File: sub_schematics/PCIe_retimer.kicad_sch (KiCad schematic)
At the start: 1 part, among them U1 DS160PT801ACBR

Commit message: buck converter
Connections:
- net PWR.1_8V: now reaches U1.AE12 (PWR_1)
- net PWR.1_8V: now also U1.AF11 (PWR_1), U1.AF13 (PWR_1), U1.AG10 (PWR_1), U1.AG14 (PWR_1), U1.AH11 (PWR_1), U1.AH13 (PWR_1), U1.AJ12 (PWR_1), U1.J12 (PWR_1), U1.K11 (PWR_1), U1.K13 (PWR_1), U1.L10 (PWR_1), U1.L14 (PWR_1), U1.M11 (PWR_1), U1.M13 (PWR_1), U1.N12 (PWR_1)
- net PWR.1_17V: now reaches U1.AA12 (PWR2_HS_D)
- net PWR.1_17V: now also U1.AB15 (PWR_2_A), U1.AB17 (PWR_2_A), U1.AB7 (PWR2_HS_A), U1.AB9 (PWR2_HS_A), U1.AC10 (PWR2_HS_D), U1.AC14 (PWR_2_A), U1.AD15 (PWR_2_A), U1.AD17 (PWR_2_A), U1.AD7 (PWR2_HS_A), U1.AD9 (PWR2_HS_A), U1.AK15 (PWR2_HS_D), U1.AK17 (PWR2_HS_A), U1.AK7 (PWR2_HS_A), U1.AK9 (PWR2_HS_D), U1.AL10 (PWR2_HS_D), U1.AL14 (PWR2_HS_D), U1.AM15 (PWR2_HS_D), U1.AM17 (PWR2_HS_A), U1.AM7 (PWR2_HS_A), U1.AM9 (PWR2_HS_D), U1.F15 (PWR2_HS_D), U1.F17 (PWR2_HS_A), U1.F7 (PWR2_HS_A), U1.F9 (PWR2_HS_D), U1.G10 (PWR2_HS_D), U1.G14 (PWR2_HS_D), U1.H15 (PWR2_HS_D), U1.H17 (PWR2_HS_A), U1.H7 (PWR2_HS_A), U1.H9 (PWR2_HS_D), U1.P15 (PWR2_HS_A), U1.P17 (PWR2_HS_A), U1.P7 (PWR_2_A), U1.P9 (PWR_2_A), U1.R10 (PWR_2_A), U1.R14 (PWR2_HS_D), U1.T15 (PWR2_HS_A), U1.T17 (PWR2_HS_A), U1.T7 (PWR_2_A), U1.T9 (PWR_2_A), U1.U12 (PWR2_HS_D), U1.V11 (PWR2_HS_D), U1.V13 (PWR2_HS_A), U1.W10 (PWR2_HS_A), U1.W14 (PWR2_HS_A), U1.Y11 (PWR2_HS_A), U1.Y13 (PWR2_HS_D)
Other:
- sheet PCIe_retimer_power ports: added PWR{1_8V 1_17V}, PWR{3V3 5V}; removed none
- moved on the sheet: U1C, U1F

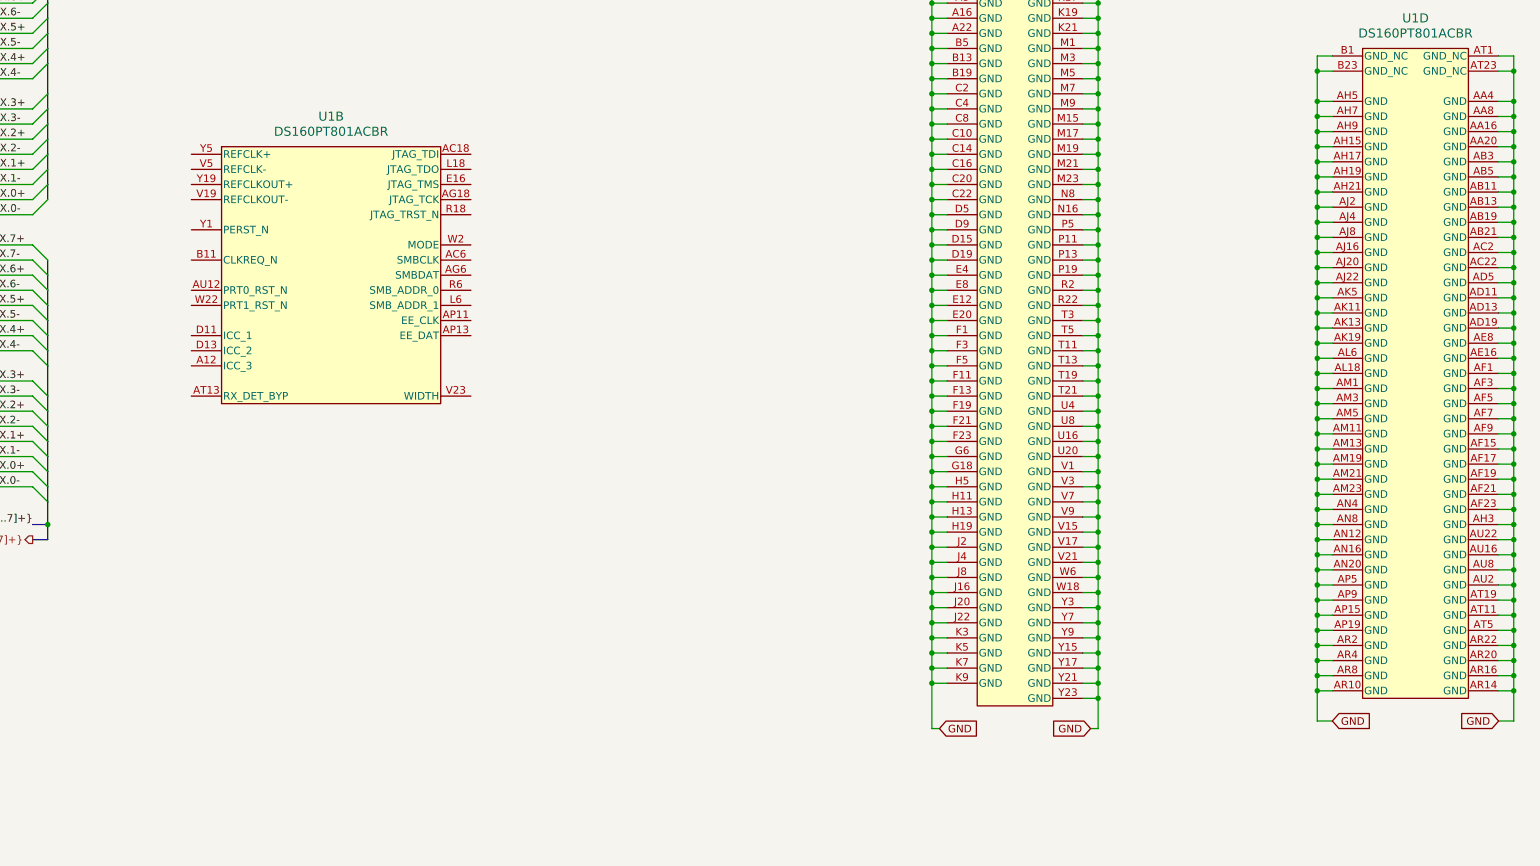
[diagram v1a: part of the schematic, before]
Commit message: Schematics revamped
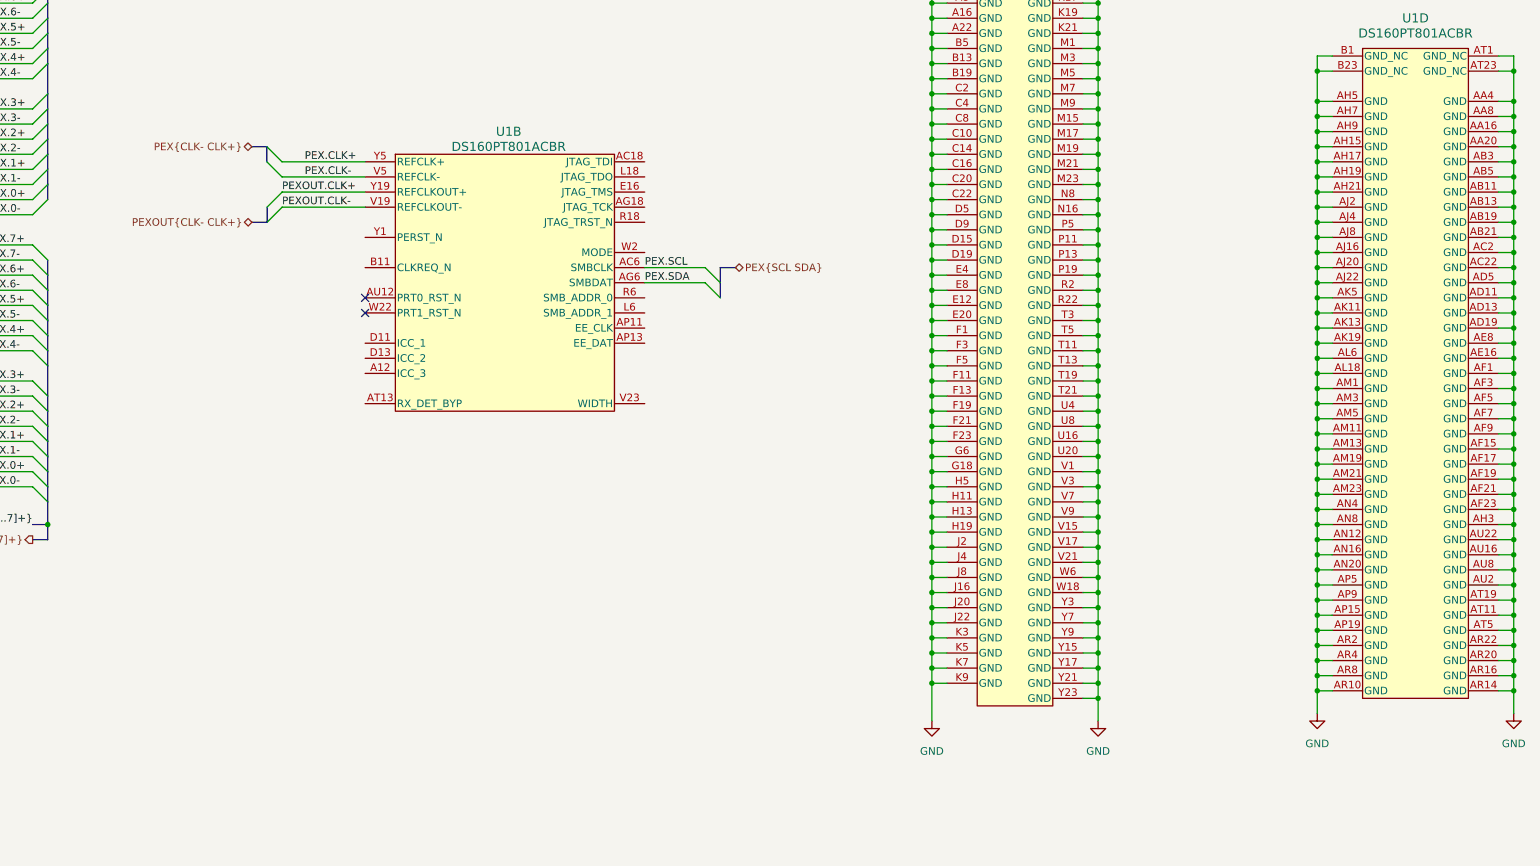
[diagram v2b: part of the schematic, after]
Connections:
- net PEX.SCL: now reaches U1.AC6 (SMBCLK)
- net PEX.SDA: now reaches U1.AG6 (SMBDAT)
- net PEXOUT.CLK-: now reaches U1.V19 (REFCLKOUT-)
- net PEX.CLK-: now reaches U1.V5 (REFCLK-)
- net PEXOUT.CLK+: now reaches U1.Y19 (REFCLKOUT+)
- net PEX.CLK+: now reaches U1.Y5 (REFCLK+)
- no-connect marks 0 -> 2
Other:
- moved on the sheet: U1B

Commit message: PCIe shematic fix
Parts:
- added C1, C10, C11, C12, C13, C14, C15, C16, C17, C18, C19, C2, C20, C21, C22, C23, C24, C25, C26, C27, C28, C29, C3, C30, C31, C32, C33, C34, C35, C36, C37, C38, C39, C4, C40, C41, C42, C43, C44, C45, C46, C47, C48, C49, C5, C50, C51, C52, C53, C54, C55, C56, C57, C58, C59, C6, C60, C61, C62, C63, C64, C7, C8, C9: 0201_885012104006, WE_WCAP-CSGP:C_Wurth_WCAP-CSGP-0201, symbol WE_WCAP-CSGP:0201_885012104006
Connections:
- net A_RX.0+: now also U1.AK21 (A_PEX_RX7N), C47.1; no longer U1.B15 (A_PEX_RX0P)
- net A_RX.0-: now also U1.AL20 (A_PEX_RX7P), C48.1; no longer U1.A14 (A_PEX_RX0N)
- net A_RX.1+: now also U1.AG22 (A_PEX_RX6N), C45.1; no longer U1.C18 (A_PEX_RX1P)
- net A_RX.1-: now also U1.AH23 (A_PEX_RX6P), C46.1; no longer U1.D17 (A_PEX_RX1N)
- net A_RX.2+: now also U1.AD21 (A_PEX_RX5N), C43.1; no longer U1.B21 (A_PEX_RX2P)
- net A_RX.2-: now also U1.AE20 (A_PEX_RX5P), C44.1; no longer U1.A20 (A_PEX_RX2N)
- net A_RX.3+: now also U1.AA22 (A_PEX_RX4N), C41.1; no longer U1.E22 (A_PEX_RX3P)
- net A_RX.3-: now also U1.AB23 (A_PEX_RX4P), C42.1; no longer U1.D23 (A_PEX_RX3N)
- net A_RX.4+: now also U1.D23 (A_PEX_RX3N), C39.1; no longer U1.AB23 (A_PEX_RX4P)
- net A_RX.4-: now also U1.E22 (A_PEX_RX3P), C40.1; no longer U1.AA22 (A_PEX_RX4N)
- net A_RX.5+: now also U1.A20 (A_PEX_RX2N), C37.1; no longer U1.AE20 (A_PEX_RX5P)
- net A_RX.5-: now also U1.B21 (A_PEX_RX2P), C38.1; no longer U1.AD21 (A_PEX_RX5N)
- net A_RX.6+: now also U1.D17 (A_PEX_RX1N), C35.1; no longer U1.AH23 (A_PEX_RX6P)
- net A_RX.6-: now also U1.C18 (A_PEX_RX1P), C36.1; no longer U1.AG22 (A_PEX_RX6N)
- net A_RX.7+: now also U1.A14 (A_PEX_RX0N), C33.1; no longer U1.AL20 (A_PEX_RX7P)
- net A_RX.7-: now also U1.B15 (A_PEX_RX0P), C34.1; no longer U1.AK21 (A_PEX_RX7N)
- net A_TX.0+: now also C2.1
- net A_TX.0-: now also C1.1
- net A_TX.1+: now also C4.1
- net A_TX.1-: now also C3.1
- net A_TX.2+: now also C6.1
- net A_TX.2-: now also C5.1
- net A_TX.3+: now also C8.1
- net A_TX.3-: now also C7.1
- net A_TX.4+: now also C10.1
- net A_TX.4-: now also C9.1
- net A_TX.5+: now also C12.1
- net A_TX.5-: now also C11.1
- net A_TX.6+: now also C14.1
- net A_TX.6-: now also C13.1
- net A_TX.7+: now also C16.1
- net A_TX.7-: now also C15.1
- net B_RX.0+: now also U1.H3 (B_PEX_RX0P), C50.1; no longer U1.H21 (B_PEX_TX0P)
- net B_RX.0-: now also U1.G4 (B_PEX_RX0N), C49.1; no longer U1.G20 (B_PEX_TX0N)
- net B_RX.1+: now also U1.L2 (B_PEX_RX1P), C52.1; no longer U1.L22 (B_PEX_TX1P)
- net B_RX.1-: now also U1.K1 (B_PEX_RX1N), C51.1; no longer U1.K23 (B_PEX_TX1N)
- net B_RX.2+: now also U1.P3 (B_PEX_RX2P), C54.1; no longer U1.P21 (B_PEX_TX2P)
- net B_RX.2-: now also U1.N4 (B_PEX_RX2N), C53.1; no longer U1.N20 (B_PEX_TX2N)
- net B_RX.3+: now also U1.U2 (B_PEX_RX3P), C56.1; no longer U1.U22 (B_PEX_TX3P)
- net B_RX.3-: now also U1.T1 (B_PEX_RX3N), C55.1; no longer U1.T23 (B_PEX_TX3N)
- net B_RX.4+: now also U1.AP1 (B_PEX_RX4P), C58.1; no longer U1.AP23 (B_PEX_TX4P)
- net B_RX.4-: now also U1.AN2 (B_PEX_RX4N), C57.1; no longer U1.AN22 (B_PEX_TX4N)
- net B_RX.5+: now also U1.AU4 (B_PEX_RX5P), C60.1; no longer U1.AU20 (B_PEX_TX4P)
- net B_RX.5-: now also U1.AT3 (B_PEX_RX5N), C59.1; no longer U1.AT21 (B_PEX_TX5N)
- net B_RX.6+: now also U1.AP7 (B_PEX_RX6P), C62.1; no longer U1.AP17 (B_PEX_TX6P)
- net B_RX.6-: now also U1.AR6 (B_PEX_RX6N), C61.1; no longer U1.AR18 (B_PEX_TX6N)
- net B_RX.7+: now also U1.AU10 (B_PEX_RX7P), C64.1; no longer U1.AU14 (B_PEX_TX7P)
- net B_RX.7-: now also U1.AT9 (B_PEX_RX7N), C63.1; no longer U1.AT15 (B_PEX_TX7N)
- net B_TX.0+: now also U1.H21 (B_PEX_TX0P), C18.1; no longer U1.H3 (B_PEX_RX0P)
- net B_TX.0-: now also U1.G20 (B_PEX_TX0N), C17.1; no longer U1.G4 (B_PEX_RX0N)
- net B_TX.1+: now also U1.L22 (B_PEX_TX1P), C20.1; no longer U1.L2 (B_PEX_RX1P)
- net B_TX.1-: now also U1.K23 (B_PEX_TX1N), C19.1; no longer U1.K1 (B_PEX_RX1N)
- net B_TX.2+: now also U1.P21 (B_PEX_TX2P), C22.1; no longer U1.P3 (B_PEX_RX2P)
- net B_TX.2-: now also U1.N20 (B_PEX_TX2N), C21.1; no longer U1.N4 (B_PEX_RX2N)
- net B_TX.3+: now also U1.U22 (B_PEX_TX3P), C24.1; no longer U1.U2 (B_PEX_RX3P)
- net B_TX.3-: now also U1.T23 (B_PEX_TX3N), C23.1; no longer U1.T1 (B_PEX_RX3N)
- net B_TX.4+: now also U1.AP23 (B_PEX_TX4P), C26.1; no longer U1.AP1 (B_PEX_RX4P)
- net B_TX.4-: now also U1.AN22 (B_PEX_TX4N), C25.1; no longer U1.AN2 (B_PEX_RX4N)
- net B_TX.5+: now also U1.AU20 (B_PEX_TX4P), C28.1; no longer U1.AU4 (B_PEX_RX5P)
- net B_TX.5-: now also U1.AT21 (B_PEX_TX5N), C27.1; no longer U1.AT3 (B_PEX_RX5N)
- net B_TX.6+: now also U1.AP17 (B_PEX_TX6P), C30.1; no longer U1.AP7 (B_PEX_RX6P)
- net B_TX.6-: now also U1.AR18 (B_PEX_TX6N), C29.1; no longer U1.AR6 (B_PEX_RX6N)
- net B_TX.7+: now also U1.AU14 (B_PEX_TX7P), C32.1; no longer U1.AU10 (B_PEX_RX7P)
- net B_TX.7-: now also U1.AT15 (B_PEX_TX7N), C31.1; no longer U1.AT9 (B_PEX_RX7N)

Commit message: Switch to retimer for only clock
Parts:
- removed C1, C10, C11, C12, C13, C14, C15, C16, C17, C18, C19, C2, C20, C21, C22, C23, C24, C25, C26, C27, C28, C29, C3, C30, C31, C32, C33, C34, C35, C36, C37, C38, C39, C4, C40, C41, C42, C43, C44, C45, C46, C47, C48, C49, C5, C50, C51, C52, C53, C54, C55, C56, C57, C58, C59, C6, C60, C61, C62, C63, C64, C7, C8, C9: 0201_885012104006, WE_WCAP-CSGP:C_Wurth_WCAP-CSGP-0201, symbol WE_WCAP-CSGP:0201_885012104006
- removed U1: DS160PT801ACBR, pcie-redriver:ACB0332A-MFG, symbol pcie-redriver:DS160PT801ACBR
- added C1, C2, C4, C5: 0201_885012004001, WE_WCAP-CSGP:C_Wurth_WCAP-CSGP-0201, symbol WE_WCAP-CSGP:0201_885012004001
- added C3: 0402_885012105020, Capacitor_SMD_Wurth:C_Wurth_WCAP-CSGP-0402, symbol WE_WCAP-CSGP:0402_885012105020
- added U1: SY75602ATWL-TR, pcie-clk-mux:VDFN8_NNC_MCH, symbol pcie-clk-mux:SY75602ATWL-TR
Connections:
- net GND: now also U1.5 (GND)
- net PEX.CLK+: now also C1.2
- net PEX.CLK-: now also C2.2
- new net: C5.2, U1.7 (OUT1_N)
- new net: C4.1, U1.6 (OUT1_P)
- new net: C1.1, U1.1 (IN_P)
- new net: C3.2, U1.8 (VDD)
- new net: C2.1, U1.2 (IN_N)
- new net PEX_RETIME.CLK+: C4.2
- new net PEX_RETIME.CLK-: C5.1
- new net PWR.3V3: C3.1
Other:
- removed sheet PCIe_retimer_power

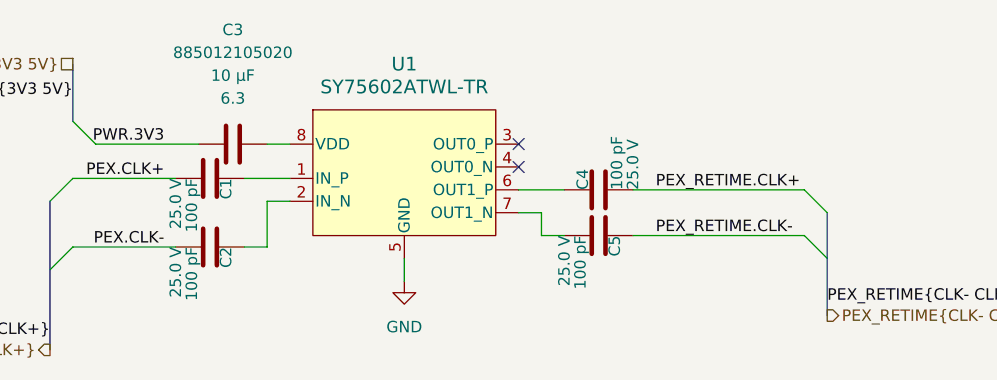
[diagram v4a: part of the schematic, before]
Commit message: Fixed board dimensions
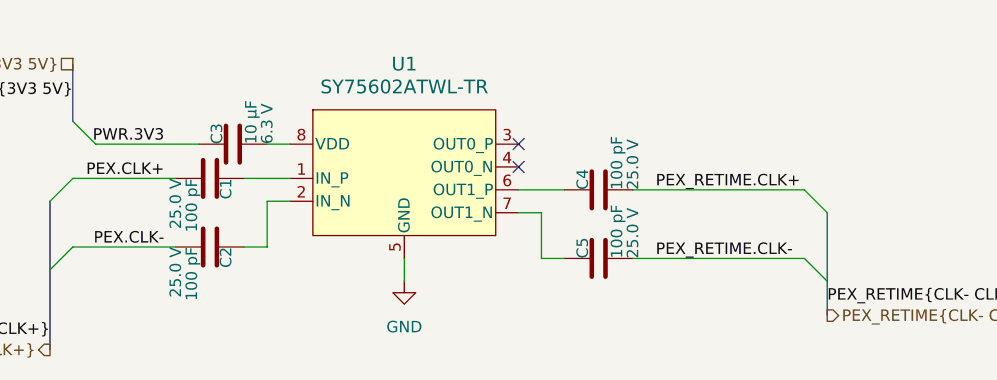
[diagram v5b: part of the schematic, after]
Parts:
- C3: footprint Capacitor_SMD_Wurth:C_Wurth_WCAP-CSGP-0402 -> WE_WCAP-CSGP:C_Wurth_WCAP-CSGP-0402; Voltage 6.3 -> 6.3 V
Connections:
- net PEX_RETIME.CLK-: now also C5.2; no longer C5.1
- net at U1.7 (OUT1_N): now also C5.1; no longer C5.2
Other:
- moved on the sheet: C5
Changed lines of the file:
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@@
 	)
 	(bus_entry
-		(at 228.6 177.8)
+		(at 228.6 180.34)
 		(size 2.54 2.54)
 		(stroke
@@
 	(wire
 		(pts
-			(xy 209.55 177.8) (xy 228.6 177.8)
+			(xy 209.55 180.34) (xy 228.6 180.34)
 		)
 		(stroke
@@
 	(wire
 		(pts
+			(xy 201.93 180.34) (xy 199.39 180.34)
+		)
+		(stroke
+			(width 0)
+			(type default)
+		)
+	)
+	(wire
+		(pts
 			(xy 168.91 173.99) (xy 171.45 173.99)
 		)
@@
 		)
 	)
+	(wire
+		(pts
+			(xy 199.39 175.26) (xy 196.85 175.26)
+		)
+		(stroke
+			(width 0)
+			(type default)
+		)
+	)
 	(bus
 		(pts
@@
 	(wire
 		(pts
-			(xy 199.39 177.8) (xy 199.39 175.26)
+			(xy 147.32 171.45) (xy 158.75 171.45)
 		)
 		(stroke
@@
 	(wire
 		(pts
-			(xy 201.93 177.8) (xy 199.39 177.8)
+			(xy 147.32 179.07) (xy 158.75 179.07)
+		)
+		(stroke
+			(width 0)
+			(type default)
+		)
+	)
+	(bus
+		(pts
+			(xy 147.32 165.1) (xy 147.32 158.75)
 		)
 		(stroke
@@
 	(wire
 		(pts
-			(xy 147.32 171.45) (xy 158.75 171.45)
+			(xy 209.55 172.72) (xy 228.6 172.72)
+		)
+		(stroke
+			(width 0)
+			(type default)
+		)
+	)
+	(wire
+		(pts
+			(xy 199.39 180.34) (xy 199.39 175.26)
+		)
+		(stroke
+			(width 0)
+			(type default)
+		)
+	)
+	(wire
+		(pts
+			(xy 166.37 179.07) (xy 168.91 179.07)
+		)
+		(stroke
+			(width 0)
+			(type default)
+		)
+	)
+	(wire
+		(pts
+			(xy 149.86 167.64) (xy 161.29 167.64)
+		)
+		(stroke
+			(width 0)
+			(type default)
+		)
+	)
+	(wire
+		(pts
+			(xy 168.91 179.07) (xy 168.91 173.99)
 		)
 		(stroke
@@
 		(pts
 			(xy 231.14 175.26) (xy 231.14 186.69)
-		)
-		(stroke
-			(width 0)
-			(type default)
-		)
-	)
-	(wire
-		(pts
-			(xy 147.32 179.07) (xy 158.75 179.07)
-		)
-		(stroke
-			(width 0)
-			(type default)
-		)
-	)
-	(bus
-		(pts
-			(xy 147.32 165.1) (xy 147.32 158.75)
-		)
-		(stroke
-			(width 0)
-			(type default)
-		)
-	)
-	(wire
-		(pts
-			(xy 209.55 172.72) (xy 228.6 172.72)
-		)
-		(stroke
-			(width 0)
-			(type default)
-		)
-	)
-	(wire
-		(pts
-			(xy 196.85 175.26) (xy 199.39 175.26)
-		)
-		(stroke
-			(width 0)
-			(type default)
-		)
-	)
-	(wire
-		(pts
-			(xy 166.37 179.07) (xy 168.91 179.07)
-		)
-		(stroke
-			(width 0)
-			(type default)
-		)
-	)
-	(wire
-		(pts
-			(xy 149.86 167.64) (xy 161.29 167.64)
-		)
-		(stroke
-			(width 0)
-			(type default)
-		)
-	)
-	(wire
-		(pts
-			(xy 168.91 179.07) (xy 168.91 173.99)
 		)
 		(stroke
@@
 	)
 	(label "PEX_RETIME.CLK-"
-		(at 212.09 177.8 0)
+		(at 212.09 180.34 0)
 		(effects
 			(font
@@
 	(symbol
 		(lib_id "WE_WCAP-CSGP:0201_885012004001")
-		(at 205.74 177.8 270)
+		(at 205.74 180.34 90)
 		(unit 1)
 		(body_style 1)
@@
 		(fields_autoplaced yes)
 		(property "Reference" "C5"
-			(at 207.518 177.8 0)
+			(at 203.962 180.34 0)
 			(show_name no)
 			(do_not_autoplace yes)
@@
 		)
 		(property "Value" "0201_885012004001"
-			(at 228.6 182.88 0)
+			(at 182.88 175.26 0)
 			(hide yes)
 			(show_name no)
@@
 		)
 		(property "Footprint" "WE_WCAP-CSGP:C_Wurth_WCAP-CSGP-0201"
-			(at 226.06 182.88 0)
+			(at 185.42 175.26 0)
 			(hide yes)
 			(show_name no)
@@
 		)
 		(property "Datasheet" "https://www.we-online.com/catalog/datasheet/885012004001.pdf?ki"
-			(at 223.52 182.88 0)
+			(at 187.96 175.26 0)
 			(hide yes)
 			(show_name no)
@@
 		)
 		(property "Description" "MLCCs 25 V(DC)"
-			(at 205.74 177.8 0)
+			(at 205.74 180.34 0)
 			(hide yes)
 			(show_name no)
@@
 		)
 		(property "Manufacturer" "Wurth Elektronik"
-			(at 220.98 182.88 0)
+			(at 190.5 175.26 0)
 			(hide yes)
 			(show_name no)
@@
 		)
 		(property "Manufacturer URL" "https://www.we-online.com"
-			(at 218.44 182.88 0)
+			(at 193.04 175.26 0)
 			(hide yes)
 			(show_name no)
@@
 		)
 		(property "Published Date" "20251008"
-			(at 215.9 182.88 0)
+			(at 195.58 175.26 0)
 			(hide yes)
 			(show_name no)
@@
 		)
 		(property "Match Code" "WCAP-CSGP"
-			(at 213.36 182.88 0)
+			(at 198.12 175.26 0)
 			(hide yes)
 			(show_name no)
@@
 		)
 		(property "Size" "0201"
-			(at 210.82 182.88 0)
+			(at 200.66 175.26 0)
 			(hide yes)
 			(show_name no)
@@
 		)
 		(property "Mounting Technology" "SMT"
-			(at 208.28 182.88 0)
+			(at 203.2 175.26 0)
 			(hide yes)
 			(show_name no)
@@
 		)
 		(property "Part Number" "885012004001"
-			(at 208.28 182.88 0)
+			(at 203.2 175.26 0)
 			(hide yes)
 			(show_name no)
@@
 		)
 		(property "Capacitance" "100 pF"
-			(at 203.708 177.8 0)
+			(at 207.772 180.34 0)
 			(show_name no)
 			(do_not_autoplace yes)
@@
 		)
 		(property "Voltage" "25.0 V"
-			(at 201.93 177.8 0)
+			(at 209.55 180.34 0)
 			(show_name no)
 			(do_not_autoplace yes)
@@
 		)
 		(property "C" "100 pF"
-			(at 203.2 190.5 0)
+			(at 208.28 167.64 0)
 			(hide yes)
 			(show_name no)
@@
 		)
 		(property "Tol. C" "±5%"
-			(at 200.66 190.5 0)
+			(at 210.82 167.64 0)
 			(hide yes)
 			(show_name no)
@@
 		)
 		(property "VR (V (DC))" "25.0"
-			(at 198.12 190.5 0)
+			(at 213.36 167.64 0)
 			(hide yes)
 			(show_name no)
@@
 		)
 		(property "Operating Temperature" "-55 °C up to +125 °C"
-			(at 195.58 190.5 0)
+			(at 215.9 167.64 0)
 			(hide yes)
 			(show_name no)
@@
 		)
 		(property "DF (%)" "–"
-			(at 193.04 190.5 0)
+			(at 218.44 167.64 0)
 			(hide yes)
 			(show_name no)
@@
 		)
 		(property "RISO" "10 GΩ"
-			(at 190.5 190.5 0)
+			(at 220.98 167.64 0)
 			(hide yes)
 			(show_name no)
@@
 		)
 		(property "Ceramic Type" "NP0 Class I"
-			(at 187.96 190.5 0)
+			(at 223.52 167.64 0)
 			(hide yes)
 			(show_name no)
@@
 		)
 		(property "L (mm)" "0.6"
-			(at 185.42 190.5 0)
+			(at 226.06 167.64 0)
 			(hide yes)
 			(show_name no)
@@
 		)
 		(property "W (mm)" "0.3"
-			(at 182.88 190.5 0)
+			(at 228.6 167.64 0)
 			(hide yes)
 			(show_name no)
@@
 		)
 		(property "H (mm)" "0.3"
-			(at 180.34 190.5 0)
+			(at 231.14 167.64 0)
 			(hide yes)
 			(show_name no)
@@
 		)
 		(property "Fl (mm)" "0.15"
-			(at 177.8 190.5 0)
+			(at 233.68 167.64 0)
 			(hide yes)
 			(show_name no)
@@
 		)
 		(property "Q (%)" "1000"
-			(at 175.26 190.5 0)
+			(at 236.22 167.64 0)
 			(hide yes)
 			(show_name no)
@@
 		)
 		(property "Demoboard" "nan"
-			(at 172.72 190.5 0)
+			(at 238.76 167.64 0)
 			(hide yes)
 			(show_name no)
@@
 		)
 		(property "Critical Parameter" ""
-			(at 198.12 177.8 0)
+			(at 213.36 180.34 0)
 			(show_name no)
 			(do_not_autoplace no)
@@
 		(fields_autoplaced yes)
 		(property "Reference" "C3"
-			(at 165.1 154.94 90)
-			(show_name no)
-			(do_not_autoplace no)
-			(effects
-				(font
-					(size 1.27 1.27)
-				)
+			(at 163.322 167.64 0)
+			(show_name no)
+			(do_not_autoplace yes)
+			(effects
+				(font
+					(size 1.27 1.27)
+				)
+				(justify left)
 			)
 		)
@@
 			)
 		)
-		(property "Footprint" "Capacitor_SMD_Wurth:C_Wurth_WCAP-CSGP-0402"
+		(property "Footprint" "WE_WCAP-CSGP:C_Wurth_WCAP-CSGP-0402"
 			(at 144.78 162.56 0)
 			(hide yes)
@@
 		)
 		(property "Part Number" "885012105020"
-			(at 165.1 157.48 90)
-			(show_name no)
-			(do_not_autoplace no)
-			(effects
-				(font
-					(size 1.27 1.27)
-				)
+			(at 162.56 162.56 0)
+			(hide yes)
+			(show_name no)
+			(do_not_autoplace no)
+			(effects
+				(font
+					(size 1.27 1.27)
+				)
+				(justify left)
 			)
 		)
 		(property "Capacitance" "10 µF"
-			(at 165.1 160.02 90)
-			(show_name no)
-			(do_not_autoplace no)
-			(effects
-				(font
-					(size 1.27 1.27)
-				)
-			)
-		)
-		(property "Voltage" "6.3"
-			(at 165.1 162.56 90)
-			(show_name no)
-			(do_not_autoplace no)
-			(effects
-				(font
-					(size 1.27 1.27)
-				)
-			)
-		)
+			(at 167.132 167.64 0)
+			(show_name no)
+			(do_not_autoplace yes)
+			(effects
+				(font
+					(size 1.27 1.27)
+				)
+				(justify left)
+			)
+		)
+		(property "Voltage" "6.3 V"
+			(at 168.91 167.64 0)
+			(show_name no)
+			(do_not_autoplace yes)
+			(effects
+				(font
+					(size 1.27 1.27)
+				)
+				(justify left)
+			)
+		)
